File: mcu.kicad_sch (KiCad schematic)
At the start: 39 parts, among them IC3 RP2040, U1 W25Q64JVSSIQ, Y1 ABM3B-12.000MHZ-10-1-U-T

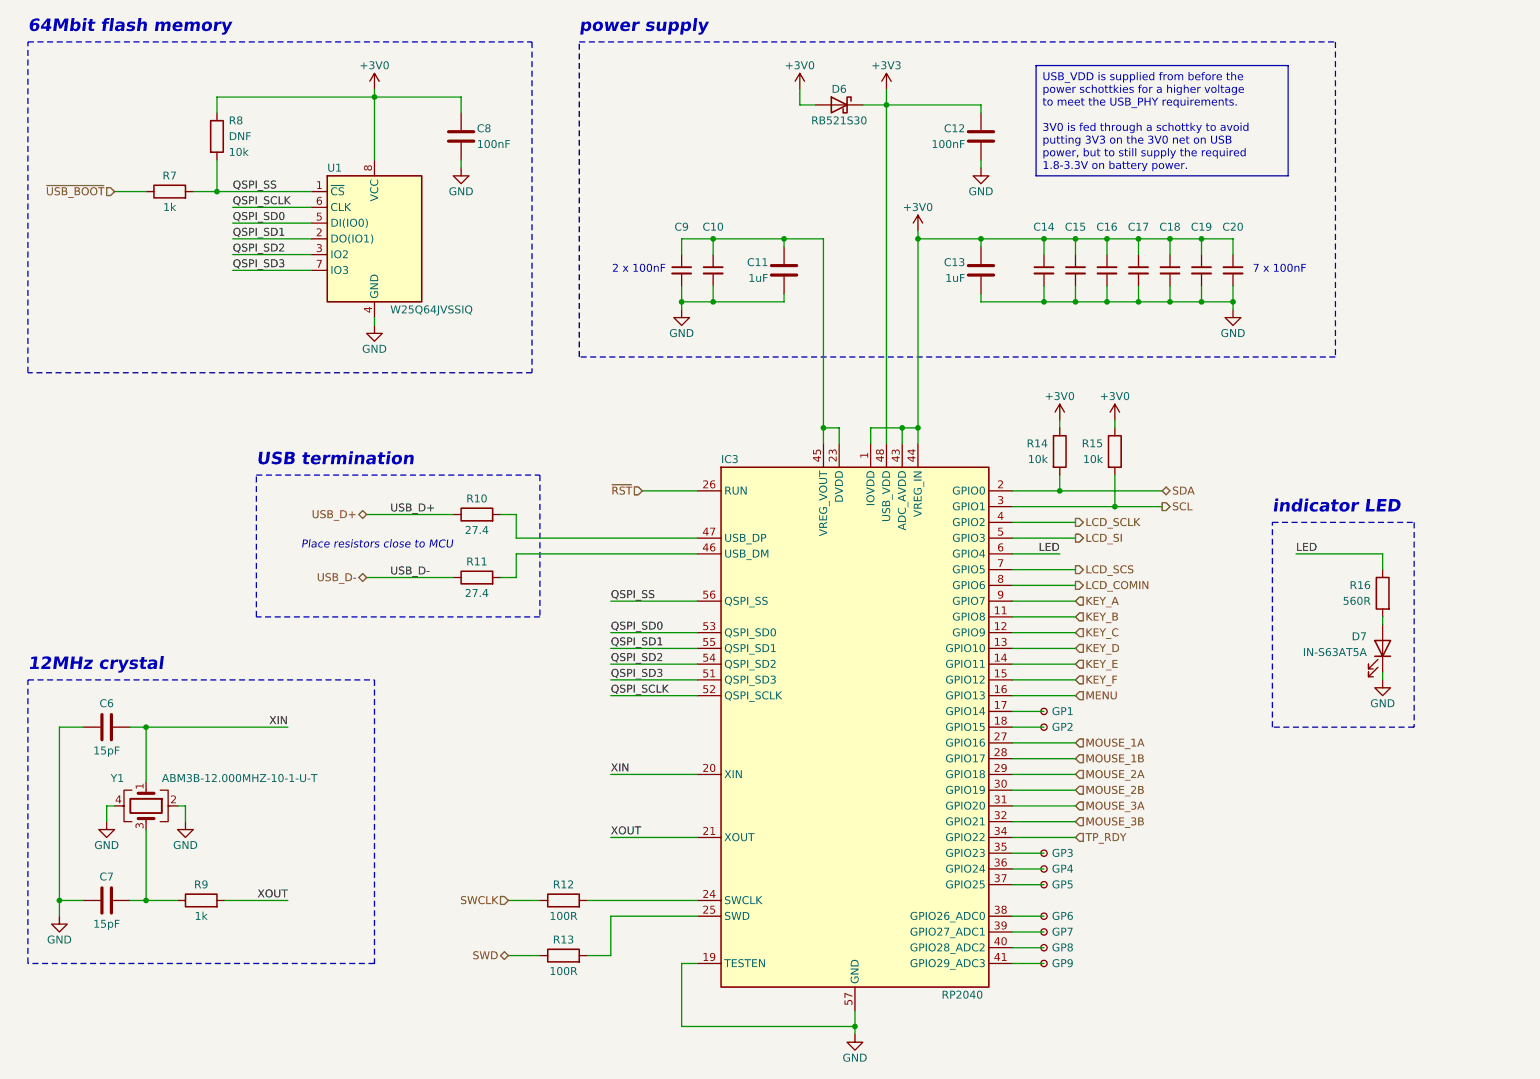
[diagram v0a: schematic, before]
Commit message: added testpoints
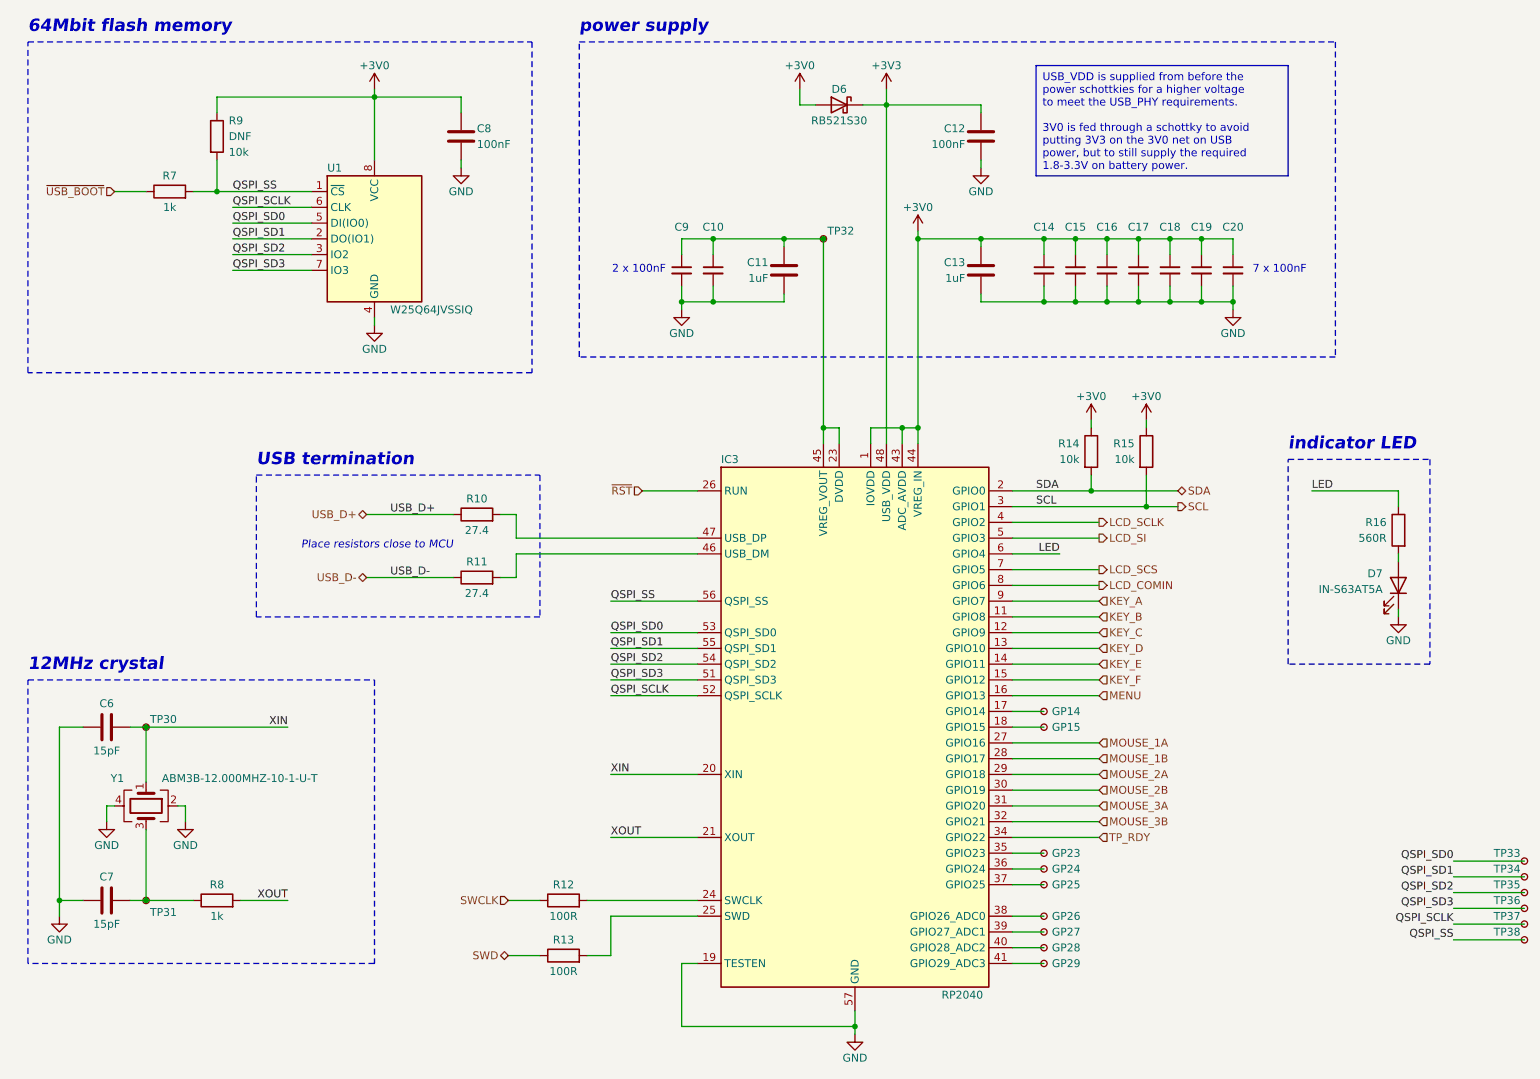
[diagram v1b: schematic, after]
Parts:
- added TP30, TP31, TP32, TP33, TP34, TP35, TP36, TP37, TP38: TestPoint_Small, TestPoint:TestPoint_Pad_D2.0mm, symbol Connector:TestPoint_Small
- renumbered GP1 to GP14, GP2 to GP15, GP3 to GP23, GP4 to GP24, GP5 to GP25, GP6 to GP26, GP7 to GP27, GP8 to GP28, GP9 to GP29, R9 to R8, R8 to R9
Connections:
- net QSPI_SCLK: now also TP37.1
- net QSPI_SD0: now also TP33.1
- net QSPI_SD1: now also TP34.1
- net QSPI_SD2: now also TP35.1
- net QSPI_SD3: now also TP36.1
- net QSPI_SS: now also TP38.1
- net XIN: now also TP30.1
- net at C10.1, C11.1, C9.1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: now also TP32.1
- net at C7.2, R8.1, Y1.3: now also TP31.1
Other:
- moved on the sheet: D7, R14, R15, R16, R8

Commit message: test points
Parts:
- removed GP14, GP15, GP23, GP24, GP25, GP26, GP27, GP28, GP29: TestPoint_Small, TestPoint:TestPoint_Pad_D2.0mm, symbol Connector:TestPoint_Small
- added TP39: GP27, TestPoint:TestPoint_Pad_D2.0mm, symbol Connector:TestPoint_Small
- added TP40: GP28, TestPoint:TestPoint_Pad_D2.0mm, symbol Connector:TestPoint_Small
- added TP41: GP29, TestPoint:TestPoint_Pad_D2.0mm, symbol Connector:TestPoint_Small
- added TP42: FD0, TestPoint:TestPoint_Pad_D2.0mm, symbol Connector:TestPoint_Small
- added TP43: FD1, TestPoint:TestPoint_Pad_D2.0mm, symbol Connector:TestPoint_Small
- added TP44: FD2, TestPoint:TestPoint_Pad_D2.0mm, symbol Connector:TestPoint_Small
- added TP45: FD3, TestPoint:TestPoint_Pad_D2.0mm, symbol Connector:TestPoint_Small
- added TP46: FCL, TestPoint:TestPoint_Pad_D2.0mm, symbol Connector:TestPoint_Small
- added TP47: FCS, TestPoint:TestPoint_Pad_D2.0mm, symbol Connector:TestPoint_Small
- TP30: value TestPoint_Small -> uXI
- TP31: value TestPoint_Small -> uXO
- TP33: value TestPoint_Small -> GP14
- TP34: value TestPoint_Small -> GP15
- TP35: value TestPoint_Small -> GP23
- TP36: value TestPoint_Small -> GP24
- TP37: value TestPoint_Small -> GP25
- TP38: value TestPoint_Small -> GP26
- renumbered R9 to R8, R8 to R9
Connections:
- net QSPI_SCLK: now also TP46.1; no longer TP37.1
- net QSPI_SD0: now also TP42.1; no longer TP33.1
- net QSPI_SD1: now also TP43.1; no longer TP34.1
- net QSPI_SD2: now also TP44.1; no longer TP35.1
- net QSPI_SD3: now also TP45.1; no longer TP36.1
- net at IC3.36 (GPIO24): now also TP36.1
- net at IC3.39 (GPIO27_ADC1): now also TP39.1
- net at IC3.40 (GPIO28_ADC2): now also TP40.1
- net at IC3.35 (GPIO23): now also TP35.1
- net at IC3.17 (GPIO14): now also TP33.1
- net at IC3.18 (GPIO15): now also TP34.1
- net at IC3.37 (GPIO25): now also TP37.1
- net at IC3.38 (GPIO26_ADC0): now also TP38.1
- net at IC3.41 (GPIO29_ADC3): now also TP41.1
- net QSPI_SS renamed QSPI_CS
- net QSPI_CS: now also TP47.1; no longer TP38.1
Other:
- moved on the sheet: R9

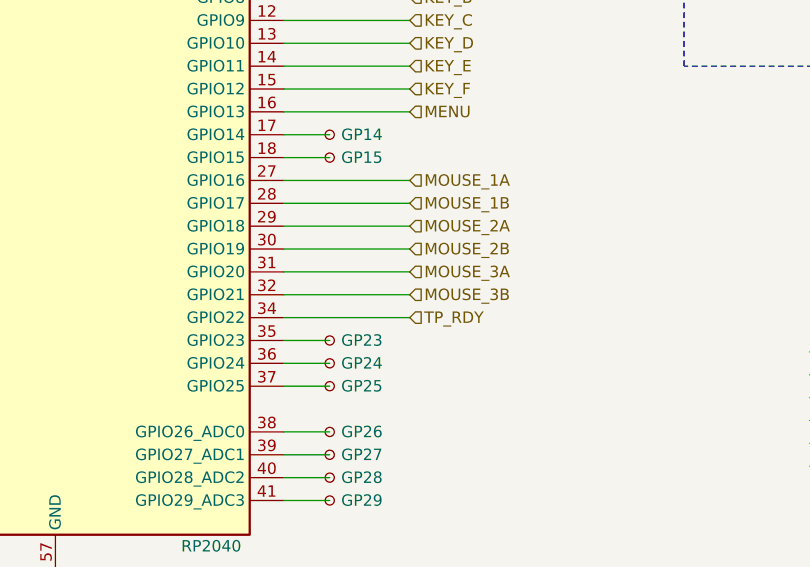
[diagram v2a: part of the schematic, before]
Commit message: finish new mouse button design
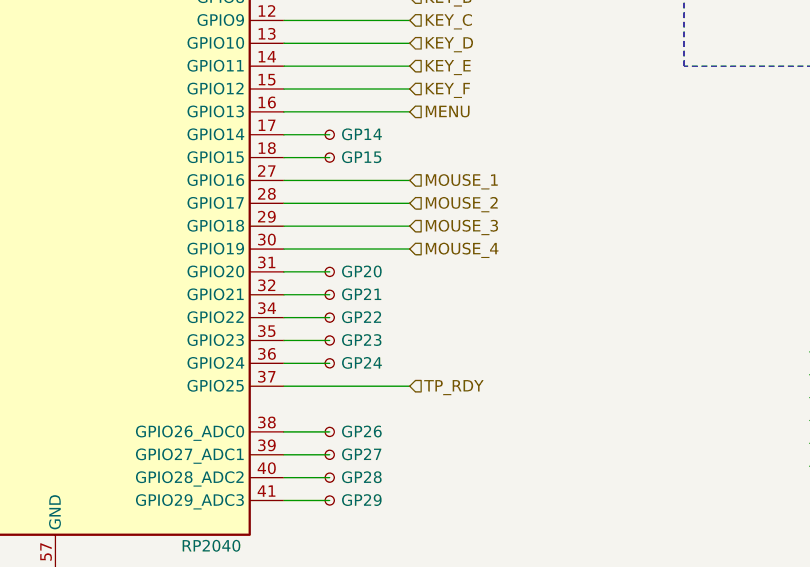
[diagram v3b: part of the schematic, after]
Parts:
- added TP50: GP21, TestPoint:TestPoint_Pad_D2.0mm, symbol Connector:TestPoint_Small
- added TP51: GP22, TestPoint:TestPoint_Pad_D2.0mm, symbol Connector:TestPoint_Small
- TP37: value GP25 -> GP20
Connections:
- net MOUSE_3A is gone; now on an unnamed net: IC3.31 (GPIO20)
- net TP_RDY: now also IC3.37 (GPIO25); no longer IC3.34 (GPIO22)
- net at TP37.1: no longer IC3.37 (GPIO25)
- net MOUSE_1A renamed MOUSE_1
- net MOUSE_1B renamed MOUSE_2
- net MOUSE_2A renamed MOUSE_3
- net MOUSE_2B renamed MOUSE_4
- net MOUSE_3B: no longer names the net of IC3.32 (GPIO21)
- net MOUSE_3B: now also TP50.1
- new net: IC3.34 (GPIO22), TP51.1
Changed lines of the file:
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@@
-    (stroke (width 0) (type default))
-  )
-  (wire (pts (xy 193.04 148.59) (xy 207.01 148.59))
     (stroke (width 0) (type default))
   )
@@
     (stroke (width 0) (type default))
   )
+  (wire (pts (xy 193.04 153.67) (xy 198.12 153.67))
+    (stroke (width 0) (type default))
+  )
   (wire (pts (xy 90.17 69.85) (xy 90.17 71.12))
     (stroke (width 0) (type default))
@@
     (stroke (width 0) (type default))
   )
-  (wire (pts (xy 193.04 161.29) (xy 198.12 161.29))
+  (wire (pts (xy 193.04 161.29) (xy 207.01 161.29))
     (stroke (width 0) (type default))
   )
@@
     (stroke (width 0) (type default))
   )
+  (wire (pts (xy 193.04 148.59) (xy 198.12 148.59))
+    (stroke (width 0) (type default))
+  )
   (wire (pts (xy 208.28 57.15) (xy 213.36 57.15))
     (stroke (width 0) (type default))
@@
     (stroke (width 0) (type default))
   )
-  (wire (pts (xy 193.04 151.13) (xy 207.01 151.13))
-    (stroke (width 0) (type default))
-  )
   (wire (pts (xy 223.52 57.15) (xy 223.52 59.69))
     (stroke (width 0) (type default))
@@
     (stroke (width 0) (type default))
   )
-  (wire (pts (xy 193.04 153.67) (xy 207.01 153.67))
-    (stroke (width 0) (type default))
-  )
   (wire (pts (xy 213.36 67.31) (xy 208.28 67.31))
     (stroke (width 0) (type default))
@@
   )
   (wire (pts (xy 162.56 87.63) (xy 162.56 57.15))
+    (stroke (width 0) (type default))
+  )
+  (wire (pts (xy 193.04 151.13) (xy 198.12 151.13))
     (stroke (width 0) (type default))
   )
@@
     (effects (font (size 1.27 1.27)) (justify left))
   )
-  (hierarchical_label "MOUSE_1A" (shape input) (at 207.01 138.43 0) (fields_autoplaced)
+  (hierarchical_label "MOUSE_1" (shape input) (at 207.01 138.43 0) (fields_autoplaced)
     (effects (font (size 1.27 1.27)) (justify left))
   )
@@
     (effects (font (size 1.27 1.27)) (justify left))
   )
-  (hierarchical_label "TP_RDY" (shape input) (at 207.01 153.67 0) (fields_autoplaced)
-    (effects (font (size 1.27 1.27)) (justify left))
-  )
-  (hierarchical_label "MOUSE_2B" (shape input) (at 207.01 146.05 0) (fields_autoplaced)
+  (hierarchical_label "TP_RDY" (shape input) (at 207.01 161.29 0) (fields_autoplaced)
     (effects (font (size 1.27 1.27)) (justify left))
   )
@@
     (effects (font (size 1.27 1.27)) (justify left))
   )
-  (hierarchical_label "MOUSE_2A" (shape input) (at 207.01 143.51 0) (fields_autoplaced)
+  (hierarchical_label "MOUSE_2" (shape input) (at 207.01 140.97 0) (fields_autoplaced)
     (effects (font (size 1.27 1.27)) (justify left))
   )
@@
     (effects (font (size 1.27 1.27)) (justify left))
   )
-  (hierarchical_label "MOUSE_3A" (shape input) (at 207.01 148.59 0) (fields_autoplaced)
+  (hierarchical_label "MOUSE_4" (shape input) (at 207.01 146.05 0) (fields_autoplaced)
     (effects (font (size 1.27 1.27)) (justify left))
   )
@@
     (effects (font (size 1.27 1.27)) (justify right))
   )
-  (hierarchical_label "MOUSE_1B" (shape input) (at 207.01 140.97 0) (fields_autoplaced)
+  (hierarchical_label "MOUSE_3" (shape input) (at 207.01 143.51 0) (fields_autoplaced)
     (effects (font (size 1.27 1.27)) (justify left))
   )
@@
   )
   (hierarchical_label "LCD_SCLK" (shape output) (at 207.01 102.87 0) (fields_autoplaced)
-    (effects (font (size 1.27 1.27)) (justify left))
-  )
-  (hierarchical_label "MOUSE_3B" (shape input) (at 207.01 151.13 0) (fields_autoplaced)
     (effects (font (size 1.27 1.27)) (justify left))
   )
@@
     )
   )
-  (symbol (lib_id "Connector:TestPoint_Small") (at 198.12 161.29 0) (unit 1)
-    (in_bom yes) (on_board yes) (dnp no)
-    (property "Reference" "TP37" (at 198.755 160.02 0)
+  (symbol (lib_id "Connector:TestPoint_Small") (at 198.12 148.59 0) (unit 1)
+    (in_bom yes) (on_board yes) (dnp no)
+    (property "Reference" "TP37" (at 198.755 147.32 0)
       (effects (font (size 1.27 1.27)) (justify left) hide)
     )
-    (property "Value" "GP25" (at 199.39 161.29 0)
-      (effects (font (size 1.27 1.27)) (justify left))
-    )
-    (property "Footprint" "TestPoint:TestPoint_Pad_D2.0mm" (at 203.2 161.29 0)
-      (effects (font (size 1.27 1.27)) hide)
-    )
-    (property "Datasheet" "~" (at 203.2 161.29 0)
+    (property "Value" "GP20" (at 199.39 148.59 0)
+      (effects (font (size 1.27 1.27)) (justify left))
+    )
+    (property "Footprint" "TestPoint:TestPoint_Pad_D2.0mm" (at 203.2 148.59 0)
+      (effects (font (size 1.27 1.27)) hide)
+    )
+    (property "Datasheet" "~" (at 203.2 148.59 0)
       (effects (font (size 1.27 1.27)) hide)
     )
@@
         (path "/ab6fff6e-44fa-4992-ab9d-8d9a7df4367d/b094ad32-9f85-443d-ad4d-e6b703944261"
           (reference "TP32") (unit 1)
+        )
+      )
+    )
+  )
+  (symbol (lib_id "Connector:TestPoint_Small") (at 198.12 153.67 0) (unit 1)
+    (in_bom yes) (on_board yes) (dnp no)
+    (property "Reference" "TP51" (at 198.755 152.4 0)
+      (effects (font (size 1.27 1.27)) (justify left) hide)
+    )
+    (property "Value" "GP22" (at 199.39 153.67 0)
+      (effects (font (size 1.27 1.27)) (justify left))
+    )
+    (property "Footprint" "TestPoint:TestPoint_Pad_D2.0mm" (at 203.2 153.67 0)
+      (effects (font (size 1.27 1.27)) hide)
+    )
+    (property "Datasheet" "~" (at 203.2 153.67 0)
+      (effects (font (size 1.27 1.27)) hide)
+    )
+    (pin "1")
+    (instances
+      (project "gkos_pebble"
+        (path "/ab6fff6e-44fa-4992-ab9d-8d9a7df4367d/b094ad32-9f85-443d-ad4d-e6b703944261"
+          (reference "TP51") (unit 1)
         )
       )
@@
         )
       )
+    )
+  )
+  (symbol (lib_id "Connector:TestPoint_Small") (at 198.12 151.13 0) (unit 1)
+    (in_bom yes) (on_board yes) (dnp no)
+    (property "Reference" "TP50" (at 198.755 149.86 0)
+      (effects (font (size 1.27 1.27)) (justify left) hide)
+    )
+    (property "Value" "GP21" (at 199.39 151.13 0)
+      (effects (font (size 1.27 1.27)) (justify left))
+    )
+    (property "Footprint" "TestPoint:TestPoint_Pad_D2.0mm" (at 203.2 151.13 0)
+      (effects (font (size 1.27 1.27)) hide)
+    )
+    (property "Datasheet" "~" (at 203.2 151.13 0)
+      (effects (font (size 1.27 1.27)) hide)
+    )
+    (pin "1")
+    (instances
+      (project "gkos_pebble"
+        (path "/ab6fff6e-44fa-4992-ab9d-8d9a7df4367d/b094ad32-9f85-443d-ad4d-e6b703944261"
+          (reference "TP50") (unit 1)
+        )
+      )
